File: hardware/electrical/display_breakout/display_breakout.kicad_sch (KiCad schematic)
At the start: 0 parts

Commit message: Updated breakout schematic
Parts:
- added J1: Conn_02x10_Odd_Even, Connector_IDC:IDC-Header_2x10_P2.54mm_Vertical, symbol Connector_Generic:Conn_02x10_Odd_Even
- added J2: Conn_01x14_Socket, symbol Connector:Conn_01x14_Socket
- added SW1: RotaryEncoder_Switch, Rotary_Encoder:RotaryEncoder_Alps_EC11E-Switch_Vertical_H20mm, symbol Device:RotaryEncoder_Switch
- added SW2, SW3: SW_Push, Button_Switch_THT:SW_TH_Tactile_Omron_B3F-100x, symbol Switch:SW_Push
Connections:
- new net +3.3V: J1.2 (Pin_2), J2.14 (Pin_14), J2.7 (Pin_7)
- new net +5V: J1.4 (Pin_4)
- new net BTN1: J1.18 (Pin_18), SW2.1
- new net BTN2: J1.19 (Pin_19), SW3.1
- new net BUZ_PWM: J1.20 (Pin_20)
- new net EC11_A(CLK): J1.15 (Pin_15), SW1.A
- new net EC11_B (DT): J1.16 (Pin_16), SW1.B
- new net EC11_SW: J1.17 (Pin_17), SW1.S1
- new net GND: J1.1 (Pin_1), J2.13 (Pin_13), SW1.C, SW1.S2, SW2.2, SW3.2
- new net SPI_CLK: J1.5 (Pin_5), J2.8 (Pin_8)
- new net SPI_MISO: J1.6 (Pin_6), J2.6 (Pin_6)
- new net SPI_MOSI: J1.3 (Pin_3), J2.9 (Pin_9)
- new net TFT_CS: J1.8 (Pin_8), J2.12 (Pin_12)
- new net TFT_DC: J1.7 (Pin_7), J2.10 (Pin_10)
- new net TFT_RST: J1.10 (Pin_10), J2.11 (Pin_11)
- new net TOUCH_CLK: J1.9 (Pin_9), J2.5 (Pin_5)
- new net TOUCH_CS: J1.11 (Pin_11), J2.4 (Pin_4)
- new net TOUCH_DIN: J1.14 (Pin_14), J2.3 (Pin_3)
- new net TOUCH_DO: J1.13 (Pin_13), J2.2 (Pin_2)
- new net TOUCH_IRQ: J1.12 (Pin_12), J2.1 (Pin_1)
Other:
- note added: "Encoder and Buttons"
- note added: "From Main Control Board"
- note added: "Pin 7: LED Backlight Pin"
- note added: "To Display"

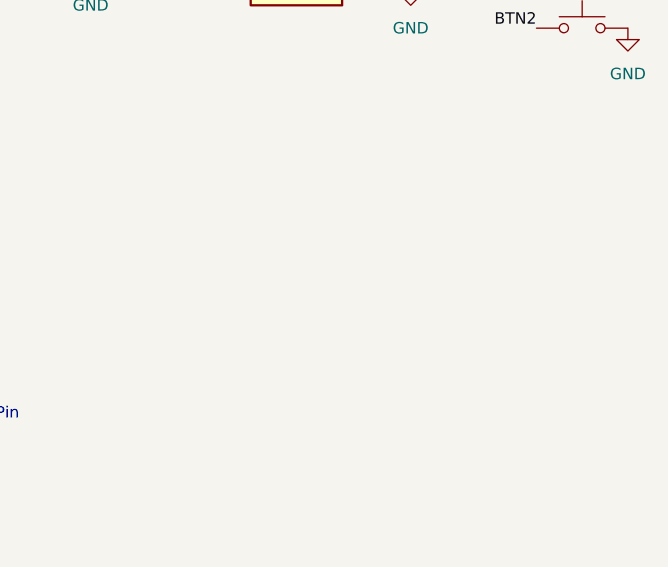
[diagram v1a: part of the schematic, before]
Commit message: included buzzer in schematic
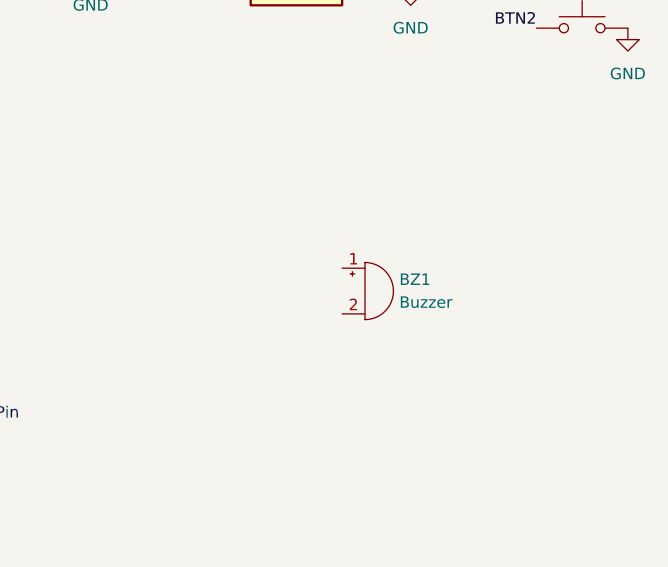
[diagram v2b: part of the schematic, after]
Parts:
- added BZ1: Buzzer, symbol Device:Buzzer
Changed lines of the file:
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@@
+	)
+	(symbol
+		(lib_id "Device:Buzzer")
+		(at 127 91.44 0)
+		(unit 1)
+		(body_style 1)
+		(exclude_from_sim no)
+		(in_bom yes)
+		(on_board yes)
+		(in_pos_files yes)
+		(dnp no)
+		(fields_autoplaced yes)
+		(property "Reference" "BZ1"
+			(at 130.81 90.1699 0)
+			(show_name no)
+			(do_not_autoplace no)
+			(effects
+				(font
+					(size 1.27 1.27)
+				)
+				(justify left)
+			)
+		)
+		(property "Value" "Buzzer"
+			(at 130.81 92.7099 0)
+			(show_name no)
+			(do_not_autoplace no)
+			(effects
+				(font
+					(size 1.27 1.27)
+				)
+				(justify left)
+			)
+		)
+		(property "Footprint" ""
+			(at 126.365 88.9 90)
+			(hide yes)
+			(show_name no)
+			(do_not_autoplace no)
+			(effects
+				(font
+					(size 1.27 1.27)
+				)
+			)
+		)
+		(property "Datasheet" ""
+			(at 126.365 88.9 90)
+			(hide yes)
+			(show_name no)
+			(do_not_autoplace no)
+			(effects
+				(font
+					(size 1.27 1.27)
+				)
+			)
+		)
+		(property "Description" "Buzzer, polarized"
+			(at 127 91.44 0)
+			(hide yes)
+			(show_name no)
+			(do_not_autoplace no)
+			(effects
+				(font
+					(size 1.27 1.27)
+				)
+			)
+		)
+		(pin "1"
+		)
+		(pin "2"
+		)
+		(instances
+			(project "display_breakout"
+				(path "/45873867-1db2-46ee-bf15-a426afef4e1f"
+					(reference "BZ1")
+					(unit 1)
+				)
+			)
+		)
 	)
 	(symbol

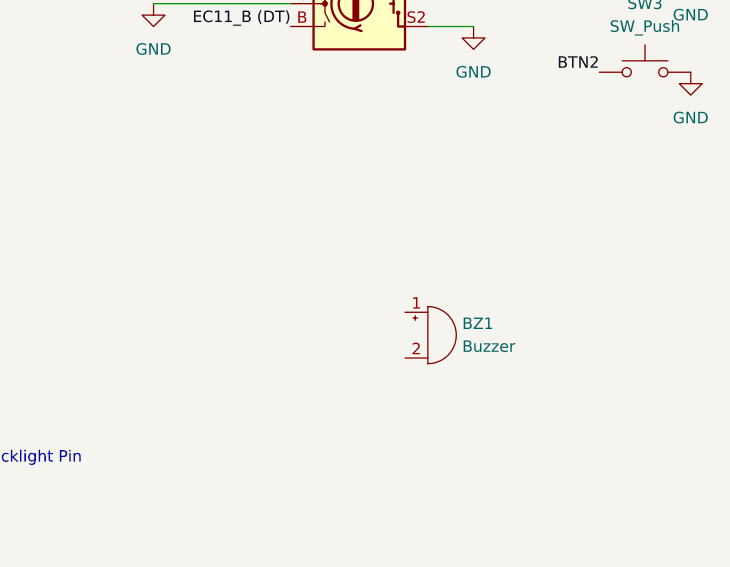
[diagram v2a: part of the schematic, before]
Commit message: updated buzzer
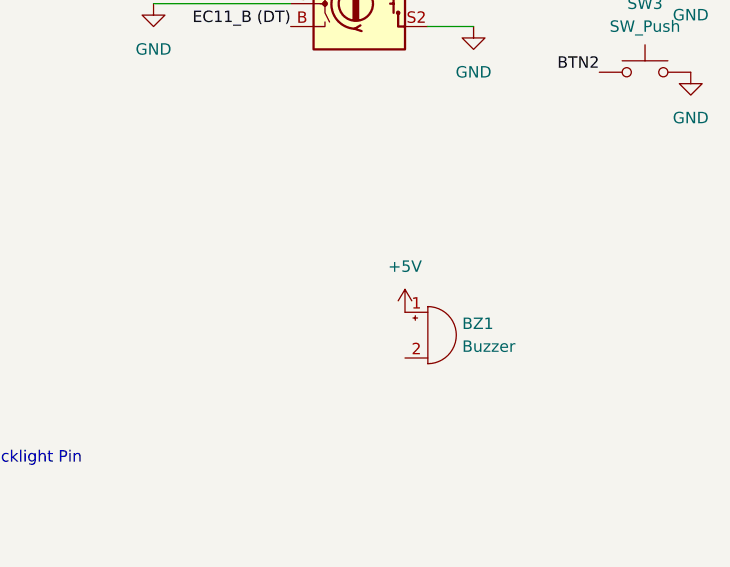
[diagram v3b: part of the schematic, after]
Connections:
- net +5V: now also BZ1.1 (+)
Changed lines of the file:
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@@
+	)
+	(symbol
+		(lib_id "power:+5V")
+		(at 124.46 88.9 0)
+		(unit 1)
+		(body_style 1)
+		(exclude_from_sim no)
+		(in_bom yes)
+		(on_board yes)
+		(in_pos_files yes)
+		(dnp no)
+		(fields_autoplaced yes)
+		(property "Reference" "#PWR05"
+			(at 124.46 92.71 0)
+			(hide yes)
+			(show_name no)
+			(do_not_autoplace no)
+			(effects
+				(font
+					(size 1.27 1.27)
+				)
+			)
+		)
+		(property "Value" "+5V"
+			(at 124.46 83.82 0)
+			(show_name no)
+			(do_not_autoplace no)
+			(effects
+				(font
+					(size 1.27 1.27)
+				)
+			)
+		)
+		(property "Footprint" ""
+			(at 124.46 88.9 0)
+			(hide yes)
+			(show_name no)
+			(do_not_autoplace no)
+			(effects
+				(font
+					(size 1.27 1.27)
+				)
+			)
+		)
+		(property "Datasheet" ""
+			(at 124.46 88.9 0)
+			(hide yes)
+			(show_name no)
+			(do_not_autoplace no)
+			(effects
+				(font
+					(size 1.27 1.27)
+				)
+			)
+		)
+		(property "Description" "Power symbol creates a global label with name \"+5V\""
+			(at 124.46 88.9 0)
+			(hide yes)
+			(show_name no)
+			(do_not_autoplace no)
+			(effects
+				(font
+					(size 1.27 1.27)
+				)
+			)
+		)
+		(pin "1"
+		)
+		(instances
+			(project "display_breakout"
+				(path "/45873867-1db2-46ee-bf15-a426afef4e1f"
+					(reference "#PWR05")
+					(unit 1)
+				)
+			)
+		)
 	)
 	(symbol

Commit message: updated schematic to latest version
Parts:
- BZ1: footprint (none) -> Buzzer_Beeper:Buzzer_12x9.5RM7.6
- J2: footprint (none) -> Connector_PinSocket_2.54mm:PinSocket_1x14_P2.54mm_Vertical
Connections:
- net BTN1: now also J1.16 (Pin_16); no longer J1.18 (Pin_18)
- net BTN2: now also J1.17 (Pin_17); no longer J1.19 (Pin_19)
- net BUZ_PWM: now also J1.18 (Pin_18); no longer J1.20 (Pin_20)
- net EC11_A(CLK): now also J1.13 (Pin_13); no longer J1.15 (Pin_15)
- net EC11_B (DT): now also J1.14 (Pin_14); no longer J1.16 (Pin_16)
- net EC11_SW: now also J1.15 (Pin_15); no longer J1.17 (Pin_17)
- net GND: now also BZ1.2 (-), J1.19 (Pin_19), J1.20 (Pin_20), J1.3 (Pin_3)
- net SPI_CLK: now also J1.7 (Pin_7); no longer J1.5 (Pin_5)
- net SPI_MOSI: now also J1.5 (Pin_5); no longer J1.3 (Pin_3)
- net TFT_DC: now also J1.9 (Pin_9); no longer J1.7 (Pin_7)
- net TOUCH_CLK: no longer J1.9 (Pin_9)
- net TOUCH_DIN: no longer J1.14 (Pin_14)
- net TOUCH_DO: no longer J1.13 (Pin_13)
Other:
- note added: "Buzzer"
